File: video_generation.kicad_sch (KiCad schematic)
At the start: 51 parts, among them J12 28L22, J13 74LS86, J14 74LS166, J15 74LS161, K0000 74LS00, K10 74LS08, K11 74LS273, K12 74LS273, K14 74LS10, K15 74LS04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

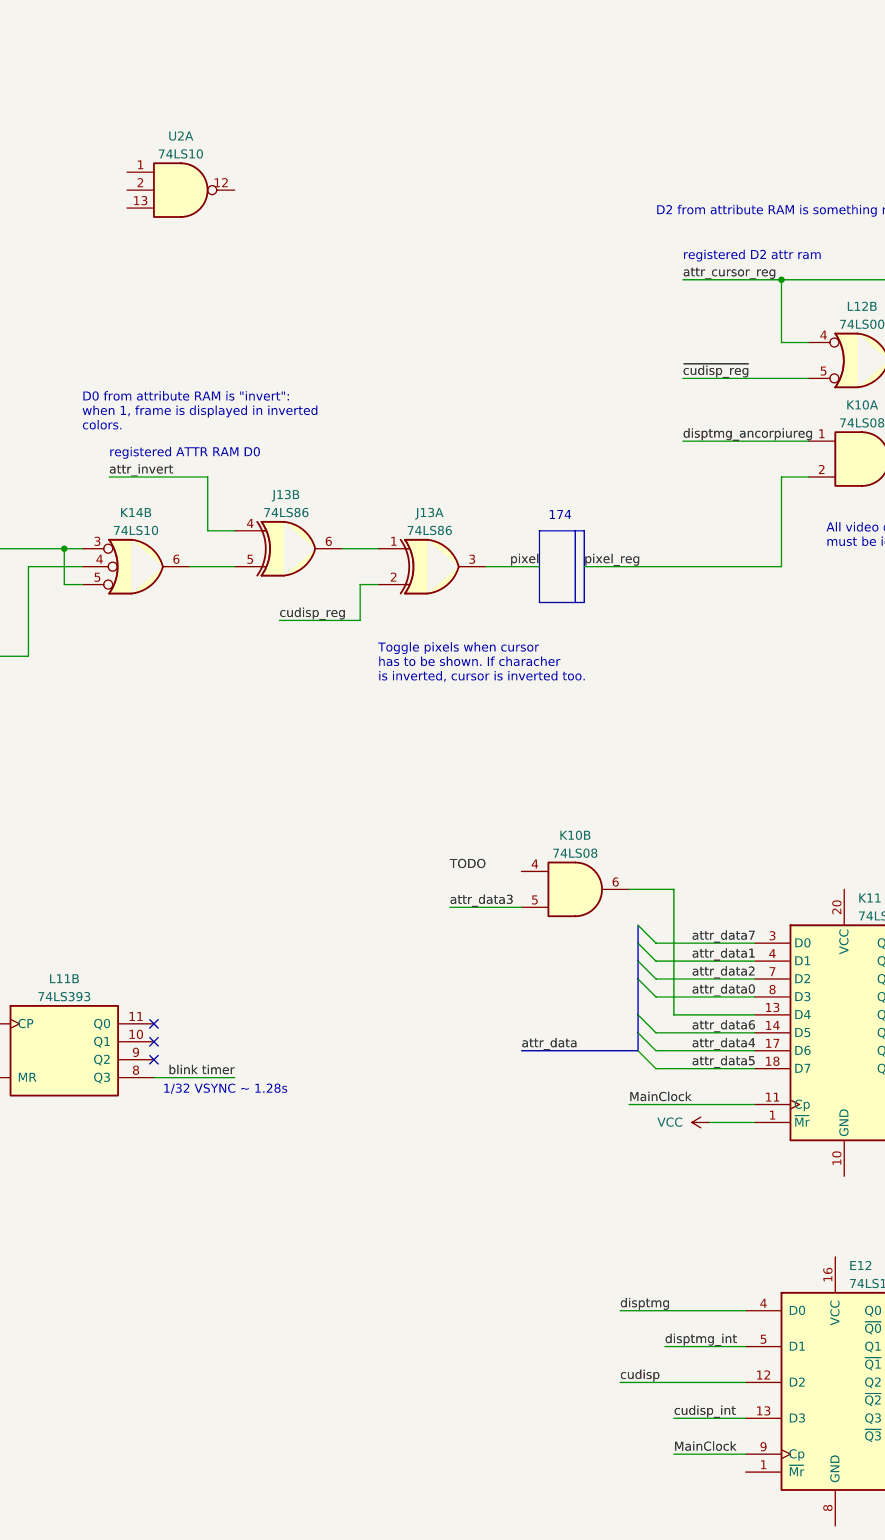
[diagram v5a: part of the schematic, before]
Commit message: Video memory concurrency
- bank7 selector to address video or attribute RAM
- found read and write data paths leading to video RAMs (F11, F12).
- video RAMs CS generation.
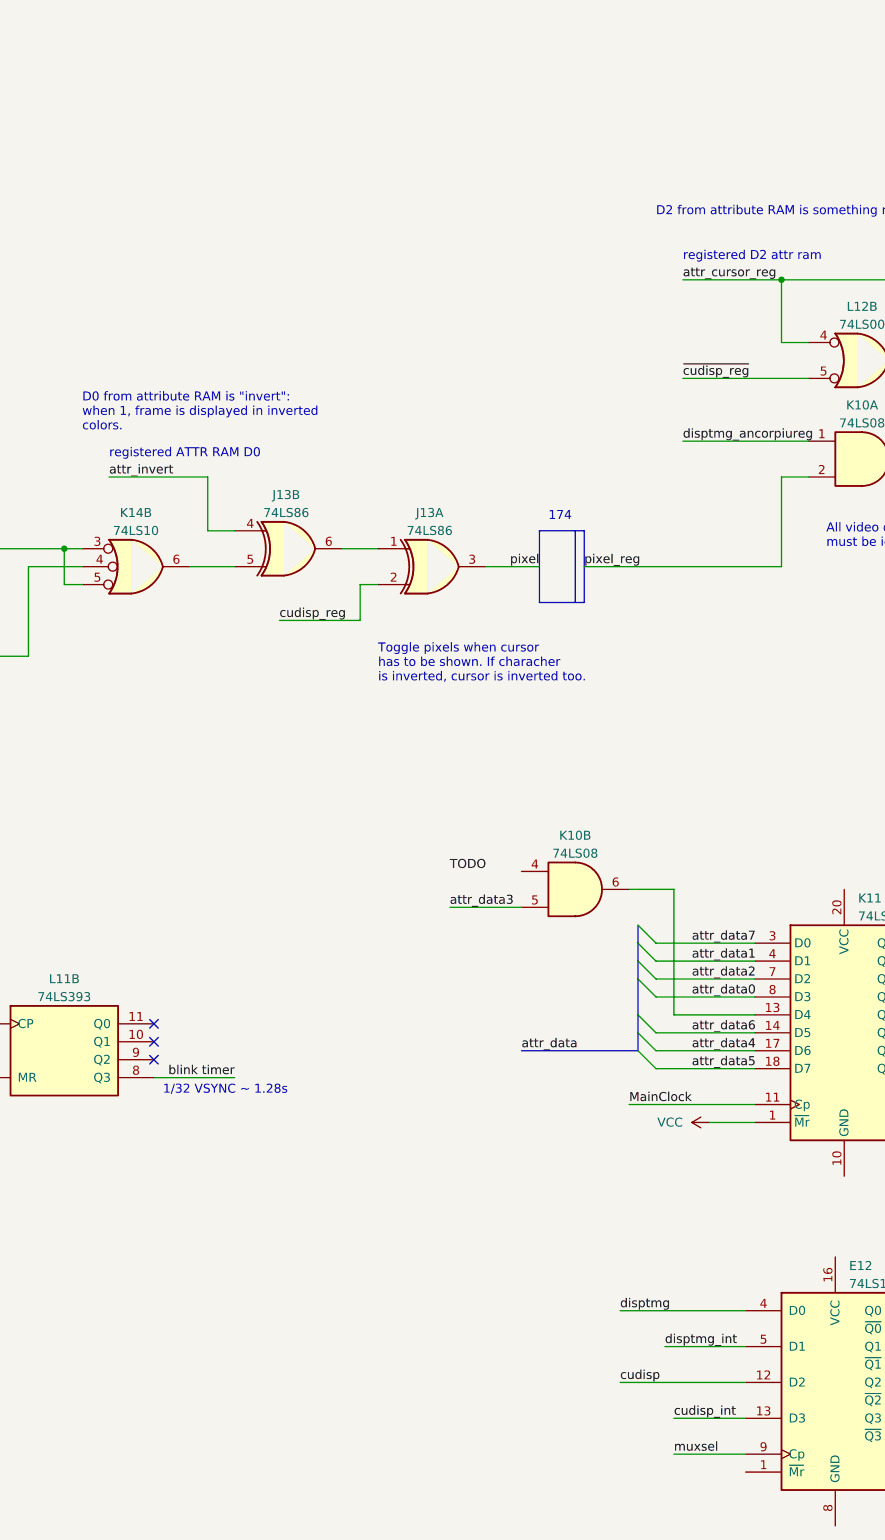
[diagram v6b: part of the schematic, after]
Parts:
- removed U2: 74LS10, symbol 74xx:74LS10
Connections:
- net MainClock: no longer E12.9 (Cp)
- new net muxsel: E12.9 (Cp)
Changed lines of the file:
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@@
-    (effects (font (size 1.27 1.27)) (justify left bottom))
-  )
-  (label "MainClock" (at 568.96 284.48 0) (fields_autoplaced)
     (effects (font (size 1.27 1.27)) (justify left bottom))
   )
@@
   )
   (label "blink timer" (at 408.94 151.13 0) (fields_autoplaced)
+    (effects (font (size 1.27 1.27)) (justify left bottom))
+  )
+  (label "muxsel" (at 568.96 284.48 0) (fields_autoplaced)
     (effects (font (size 1.27 1.27)) (justify left bottom))
   )
@@
         )
       )
-    )
-  )
-  (symbol (lib_id "74xx:74LS10") (at 499.11 105.41 0) (unit 1)
-    (in_bom yes) (on_board yes) (dnp no) (fields_autoplaced)
-    (property "Reference" "U2" (at 499.1017 97.79 0)
-      (effects (font (size 1.27 1.27)))
-    )
-    (property "Value" "74LS10" (at 499.1017 100.33 0)
-      (effects (font (size 1.27 1.27)))
-    )
-    (property "Footprint" "" (at 499.11 105.41 0)
-      (effects (font (size 1.27 1.27)) hide)
-    )
-    (property "Datasheet" "http://www.ti.com/lit/gpn/sn74LS10" (at 499.11 105.41 0)
-      (effects (font (size 1.27 1.27)) hide)
-    )
-    (pin "1")
-    (pin "12")
-    (pin "13")
-    (pin "2")
-    (pin "3")
-    (pin "4")
-    (pin "5")
-    (pin "6")
-    (pin "10")
-    (pin "11")
-    (pin "8")
-    (pin "9")
-    (pin "14")
-    (pin "7")
-    (instances
-      (project "ceda"
-        (path "/12a6dbe3-008d-4c5b-88f6-9f1c816060be/ce60e45b-d802-4380-8f39-bef3de5fa20e"
-          (reference "U2") (unit 1)
-        )
-      )

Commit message: Added some missing labels and references
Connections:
- net VCC: now also H11.1 (~{Mr})
- net attr_hide renamed attr_show
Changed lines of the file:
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@@
     (stroke (width 0) (type default))
   )
-  (wire (pts (xy 151.13 260.35) (xy 146.05 260.35))
+  (wire (pts (xy 151.13 260.35) (xy 139.7 260.35))
     (stroke (width 0) (type default))
   )
@@
     (stroke (width 0) (type default))
   )
+  (wire (pts (xy 148.59 262.89) (xy 151.13 262.89))
+    (stroke (width 0) (type default))
+  )
   (wire (pts (xy 231.14 180.34) (xy 252.73 180.34))
     (stroke (width 0) (type default))
@@
     (stroke (width 0) (type default))
   )
-  (wire (pts (xy 146.05 260.35) (xy 146.05 275.59))
+  (wire (pts (xy 139.7 260.35) (xy 139.7 274.32))
     (stroke (width 0) (type default))
   )
@@
     (stroke (width 0) (type default))
   )
-  (wire (pts (xy 146.05 275.59) (xy 142.24 275.59))
+  (wire (pts (xy 139.7 274.32) (xy 127 274.32))
     (stroke (width 0) (type default))
   )
@@
     (effects (font (size 1.27 1.27)) (justify left bottom))
   )
-  (label "attr_hide" (at 671.83 229.87 180) (fields_autoplaced)
+  (label "attr_show" (at 671.83 229.87 180) (fields_autoplaced)
     (effects (font (size 1.27 1.27)) (justify right bottom))
   )
@@
     (effects (font (size 1.27 1.27)) (justify right bottom))
   )
+  (label "attr_show" (at 435.61 158.75 0) (fields_autoplaced)
+    (effects (font (size 1.27 1.27)) (justify left bottom))
+  )
   (label "vmem0" (at 64.77 120.65 0) (fields_autoplaced)
     (effects (font (size 1.27 1.27)) (justify left bottom))
@@
     (effects (font (size 1.27 1.27)) (justify left bottom))
   )
-  (label "~{MainClock}" (at 142.24 275.59 180) (fields_autoplaced)
-    (effects (font (size 1.27 1.27)) (justify right bottom))
+  (label "~{MainClock}" (at 127 274.32 0) (fields_autoplaced)
+    (effects (font (size 1.27 1.27)) (justify left bottom))
   )
   (label "~{VSYNC_CRTC}" (at 420.37 223.52 0) (fields_autoplaced)
@@
     (effects (font (size 1.27 1.27)) (justify left bottom))
   )
-  (label "attr_hide" (at 435.61 158.75 0) (fields_autoplaced)
-    (effects (font (size 1.27 1.27)) (justify left bottom))
-  )
   (label "char5" (at 210.82 180.34 180) (fields_autoplaced)
     (effects (font (size 1.27 1.27)) (justify right bottom))
@@
         )
       )
+    )
+  )
+  (symbol (lib_id "power:VCC") (at 148.59 262.89 90) (unit 1)
+    (in_bom yes) (on_board yes) (dnp no) (fields_autoplaced)
+    (property "Reference" "#PWR050" (at 152.4 262.89 0)
+      (effects (font (size 1.27 1.27)) hide)
+    )
+    (property "Value" "VCC" (at 144.78 262.89 90)
+      (effects (font (size 1.27 1.27)) (justify left))
+    )
+    (property "Footprint" "" (at 148.59 262.89 0)
+      (effects (font (size 1.27 1.27)) hide)
+    )
+    (property "Datasheet" "" (at 148.59 262.89 0)
+      (effects (font (size 1.27 1.27)) hide)
+    )
+    (pin "1")
+    (instances
+      (project "ceda"
+        (path "/12a6dbe3-008d-4c5b-88f6-9f1c816060be/ce60e45b-d802-4380-8f39-bef3de5fa20e"
+          (reference "#PWR050") (unit 1)
+        )
+      )

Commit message: Found vsync frame signal for z80 + minors
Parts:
- added L9: 74LS109, symbol 74xx:74LS109
- added R42: 4.7k, symbol Device:R
- added U2: 74LS32, symbol 74xx:74LS32
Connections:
- net +5V: now also L9.11 (~{S}), L9.13 (~{K}), L9.14 (J)
- net VCC: now also R42.1
- net ~{VSYNC_CRTC}: now also E13.8, L13.12, L13.13
- net at E7E11.39 (HSYNC): now also E13.1; no longer E13.9
- net ~{CRTC_CS}: now reaches E7E11.25 (~{CS})
- net ~{CRTC_CS}: now also U2.9
- net at E7E11.3 (LPSTB): now also R42.2
- net VSYNC_CRTC: now reaches E7E11.40 (VSYNC)
- net VSYNC_CRTC: now also E13.9, L9.12 (C); no longer E13.1
- new net: L9.15 (~{R}), U2.8
- new net C1: L9.10 (Q)
- new net ~{RD}: U2.10
- no-connect marks 29 -> 30
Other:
- note added: "This latch is used to generate a syncronization signal, setted by the VSYNC from CRTC, resetted by a read access to CRTC from Z80."
- moved on the sheet: E13A, E13D, L13C, L13D, R68, R69
